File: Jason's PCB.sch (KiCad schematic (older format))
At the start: 17 parts, among them U1 Elite-C

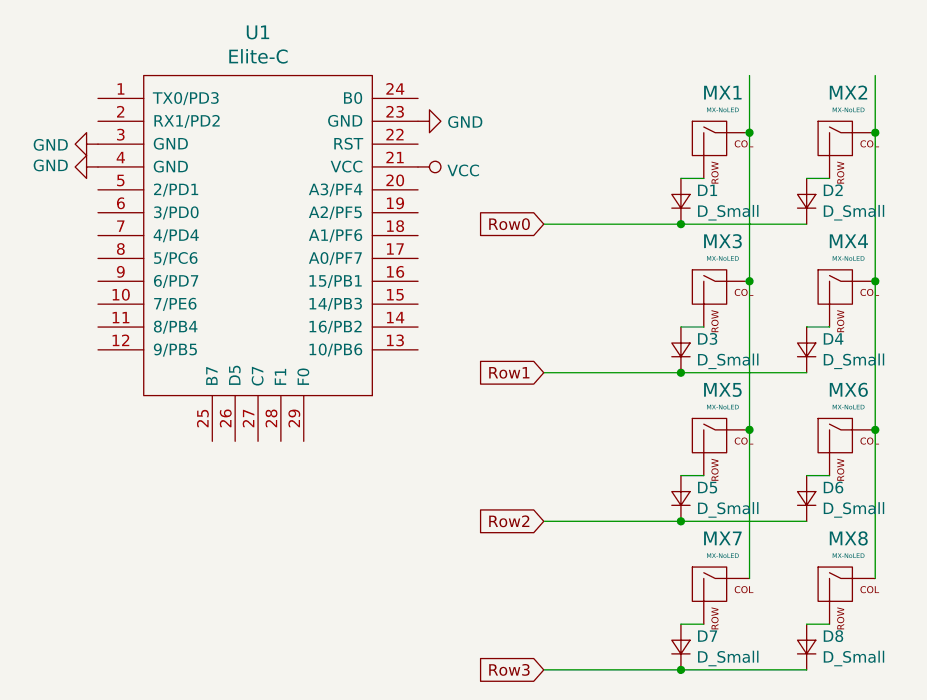
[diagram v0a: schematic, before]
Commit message: Schematic updates
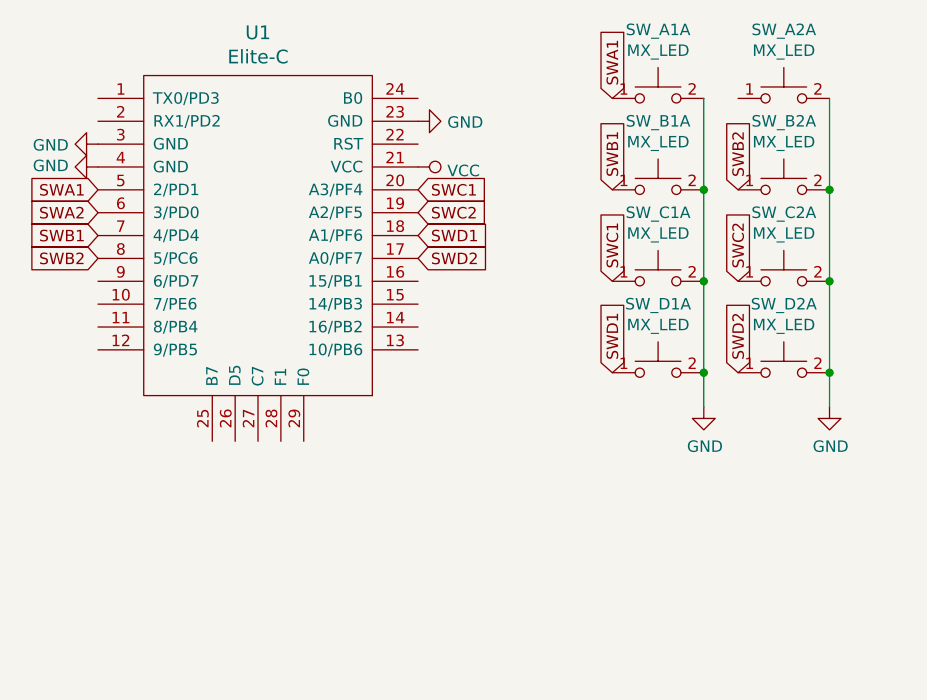
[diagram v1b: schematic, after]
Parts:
- removed D1, D2, D3, D4, D5, D6, D7, D8: D_Small, Keebio-Parts:D_SOD123, symbol Device:D_Small
- removed MX1, MX2, MX3, MX4, MX5, MX6, MX7, MX8: MX-NoLED, MX_Only:MXOnly-1U-NoLED, symbol MX_Alps_Hybrid:MX-NoLED
- added SW_A1, SW_A2, SW_B1, SW_B2, SW_C1, SW_C2, SW_D1, SW_D2: MX_LED, MX_Only:MXOnly-1U, symbol keebio:MX_LED
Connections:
- net labels added: SWA1, SWA2, SWB1, SWB2, SWC1, SWC2, SWD1, SWD2
- net labels removed: Row0, Row1, Row2, Row3
- wire segments 24 -> 8
